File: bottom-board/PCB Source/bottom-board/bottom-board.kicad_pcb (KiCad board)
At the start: 2 copper layers, 193 x 93 mm, 259 parts, among them P1 USB_B, P10 JACK_TRS_6PINS, P11 JACK_TRS_6PINS, P12 JACK_TRS_6PINS, P13 RJ45, P14 AudioJack3, P2 USB_A, P3 BARREL_JACK, P5 HMI_DATA, P6 AudioJack3, P7 AudioJack3, P8 SERIAL_DEBUG, P9 JACK_TRS_6PINS, Q1 2N7002, Q10 J110, Q12 2N7002, Q13 2N7002, Q2 2N7002, Q3 J110, Q4 J110, Q5 J110, Q6 J110, Q7 2N7002, Q8 2N7002, Q9 J110, U1 TS2596, U10 RT9742MNGJ5, U11 6N137S, U12 ISL83491, U13 AP2120N-3.3, U2 LD1117S50TR_SOT223, U3 CS4265, U4 AT24CS08-STUM, U5 LM4562, U6 TL082, U7 TL082, U8 LM4811, U9 GR30-SOM

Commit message: rev 0.0.3
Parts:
- removed FB11, FB2, FB3, FB4, FB5, FB6, FB7, FB8, FB9: Ferrite_Bead, Resistor_SMD:R_0603_1608Metric
- removed G***: LOGO, Uno:mod-logo
- removed L3: 1mH, Inductor_SMD:L_Bourns_SRR1260
- removed R72: 10K, Resistor_SMD:R_0603_1608Metric
- added C73: 100nF, Capacitor_SMD:C_0603_1608Metric, F.Cu at (220.6, 99.7)
- added C75: 100nF, Capacitor_SMD:C_0603_1608Metric, F.Cu at (229.8, 102.1)
- added C76: 10uF, Capacitor_SMD:C_0805_2012Metric, F.Cu at (228.7, 105.5)
- added C77: 100nF, Capacitor_SMD:C_0603_1608Metric, F.Cu at (228.4, 103.7)
- added C78: 10uF, Capacitor_SMD:C_0805_2012Metric, F.Cu at (231.7, 98.1)
- added C79: 100nF, Capacitor_SMD:C_0603_1608Metric, F.Cu at (221.1, 94.9)
- added C80: 10uF, Capacitor_SMD:C_0805_2012Metric, F.Cu at (219.3, 94.9)
- added C81: 100nF, Capacitor_SMD:C_0603_1608Metric, F.Cu at (229.9, 97.9)
- added C82: 100nF, Capacitor_SMD:C_0603_1608Metric, F.Cu at (190.7, 64.0)
- added C83: 47uF, Capacitor_SMD:CP_Elec_5x5.4, F.Cu at (184.8, 93.8)
- added C84: 47uF, Capacitor_SMD:CP_Elec_5x5.4, F.Cu at (174.6, 111.0)
- added C85: 100nF, Capacitor_SMD:C_0603_1608Metric, F.Cu at (113.1, 66.9)
- added C86: 100nF, Capacitor_SMD:C_0603_1608Metric, F.Cu at (115.8, 70.0)
- added C87: 100nF, Capacitor_SMD:C_0603_1608Metric, F.Cu at (171.3, 82.8)
- added C88: 10uF, Capacitor_SMD:CP_Elec_4x5.7, F.Cu at (216.1, 101.3)
- added C89: 10uF, Capacitor_SMD:CP_Elec_4x5.7, F.Cu at (216.1, 106.2)
- added C90: 100pF, Capacitor_SMD:C_0603_1608Metric, F.Cu at (216.8, 98.0)
- added C91: 100pF, Capacitor_SMD:C_0603_1608Metric, F.Cu at (213.0, 109.8)
- added C92: 1nF, Capacitor_SMD:C_0603_1608Metric, F.Cu at (147.8, 52.2)
- added C93: 1nF, Capacitor_SMD:C_0603_1608Metric, F.Cu at (119.8, 44.2)
- added C94: 100nF, Capacitor_SMD:C_0603_1608Metric, F.Cu at (230.9, 110.3)
- added D12: BAT54S, Package_TO_SOT_SMD:SOT-23, F.Cu at (191.2, 57.8)
- added D17: BAT54S, Package_TO_SOT_SMD:SOT-23, F.Cu at (106.0, 67.6)
- added D18: BAT54S, Package_TO_SOT_SMD:SOT-23, F.Cu at (115.7, 72.8)
- added D19: BAT54S, Package_TO_SOT_SMD:SOT-23, F.Cu at (201.4, 101.6)
- added D20: BAT54S, Package_TO_SOT_SMD:SOT-23, F.Cu at (206.4, 110.2)
- added D21: BAT54S, Package_TO_SOT_SMD:SOT-23, F.Cu at (192.6, 96.2)
- added D22: BAT54S, Package_TO_SOT_SMD:SOT-23, F.Cu at (199.1, 106.1)
- added H6: MountingHole_Pad, MountingHole:MountingHole_3.2mm_M3_DIN965_Pad, F.Cu at (134.7, 83.7)
- added H7: MountingHole_Pad, MountingHole:MountingHole_3.2mm_M3_DIN965_Pad, F.Cu at (71.2, 83.7)
- added J1: AS0A823-H4SB-7H, Uno:TE_2309407-1, F.Cu at (106.2, 128.3)
- added JP1: Jumper, Jumper:SolderJumper-2_P1.3mm_Bridged2Bar_RoundedPad1.0x1.5mm, F.Cu at (225.6, 104.7)
- added R100: 1k, Resistor_SMD:R_0603_1608Metric, F.Cu at (195.0, 89.5)
- added R101: 100, Resistor_SMD:R_0603_1608Metric, F.Cu at (204.2, 77.5)
- added R102: 150R, Resistor_SMD:R_0603_1608Metric, F.Cu at (192.2, 93.5)
- added R103: 6R8, Resistor_SMD:R_0603_1608Metric, F.Cu at (108.2, 56.8)
- added R104: 6R8, Resistor_SMD:R_0603_1608Metric, F.Cu at (119.5, 50.9)
- added R105: 150R, Resistor_SMD:R_0603_1608Metric, F.Cu at (194.7, 102.7)
- added R106: 150R, Resistor_SMD:R_0603_1608Metric, F.Cu at (195.6, 106.8)
- added R107: 150R, Resistor_SMD:R_0603_1608Metric, F.Cu at (198.8, 111.2)
- added R108: 150R, Resistor_SMD:R_0603_1608Metric, F.Cu at (189.7, 94.5)
- added R109: 150R, Resistor_SMD:R_0603_1608Metric, F.Cu at (193.0, 108.5)
- added R48: 1M 1%, Resistor_SMD:R_0603_1608Metric, F.Cu at (119.8, 47.3)
- added R98: 10K, Resistor_SMD:R_0603_1608Metric, F.Cu at (201.9, 105.4)
- added R99: 1k, Resistor_SMD:R_0603_1608Metric, F.Cu at (245.0, 80.0)
- added X1: 24.576MHz, Oscillator:Oscillator_SMD_Abracon_ASV-4Pin_7.0x5.1mm, F.Cu at (226.6, 110.9)
- C1: value 100nF -> 10uF; footprint Capacitor_SMD:C_0603_1608Metric -> Capacitor_SMD:CP_Elec_4x5.7
- C11: value 10uF -> 100nF; footprint Capacitor_SMD:C_0805_2012Metric -> Capacitor_SMD:C_0603_1608Metric
- C14, C35, C38: value 10uF -> 100nF
- C2: value 1000uF -> 10uF; footprint Capacitor_THT:CP_Radial_D10.0mm_P5.00mm -> Capacitor_SMD:CP_Elec_4x5.7
- C24: footprint Capacitor_SMD:C_0805_2012Metric -> Capacitor_SMD:C_0603_1608Metric
- C4: value 100nF -> 1nF
- C40, C47, C55: value 10uF -> 100pF; footprint Capacitor_SMD:CP_Elec_4x5.7 -> Capacitor_SMD:C_0603_1608Metric
- C42: value 10uF -> 47uF; footprint Capacitor_SMD:CP_Elec_4x5.7 -> Capacitor_SMD:CP_Elec_5x5.4
- C53, C6: value 1000uF -> 100nF; footprint Capacitor_THT:CP_Radial_D10.0mm_P5.00mm -> Capacitor_SMD:C_0603_1608Metric
- C56: value 100uF -> 100pF; footprint Capacitor_SMD:CP_Elec_6.3x7.7 -> Capacitor_SMD:C_0603_1608Metric
- C57: value 100uF -> 47uF; footprint Capacitor_SMD:CP_Elec_6.3x7.7 -> Capacitor_SMD:CP_Elec_5x5.4
- C61: footprint Capacitor_SMD:CP_Elec_5x5.3 -> Capacitor_SMD:CP_Elec_4x5.7
- C72: value 100nF -> 47uF; footprint Capacitor_SMD:C_0603_1608Metric -> Capacitor_SMD:CP_Elec_5x5.4
- C74: value 1000uF -> 47uF; footprint Capacitor_THT:CP_Radial_D10.0mm_P5.00mm -> Capacitor_SMD:CP_Elec_5x5.4
- D15, D16: footprint Diode_SMD:D_SOD-523 -> Diode_SMD:D_SOD-323
- D3, D4: value 1N4148 -> BAT54S; footprint Diode_SMD:D_SOD-323 -> Package_TO_SOT_SMD:SOT-23
- H1: value MountingHole_Pad -> HOLE; footprint MountingHole:MountingHole_3.2mm_M3_DIN965_Pad -> Uno:Hole_3.5mm
- Q10, Q3, Q4, Q5, Q6, Q9: value J110 -> BSR58
- R1, R11, R2: value 10k -> 2k7
- R16: value 10K -> 1M 1%
- R42: value 5K6 -> 10K
- R43: value 10k -> 15K
- R68, R69: value 10K -> 2k7
- R70, R71: value 10K -> 1k
- R8: value 10R -> 100; footprint Resistor_SMD:R_1206_3216Metric -> Resistor_SMD:R_0603_1608Metric
- R80, R82, R84: value 33R -> 10K
- R81, R83: value 22K 1% -> 10K
- R85: value 68R -> 10K
- R86: value 33R -> 150R
- R87: value 68R -> 150R
- U2: value LD1117S50TR_SOT223 -> TL750M10CKVURG3; footprint Package_TO_SOT_SMD:SOT-223-3_TabPin2 -> Package_TO_SOT_SMD:TO-252-3_TabPin2
- U6, U7: value TL082 -> OPA1678
- U9: value GR30-SOM -> LD1117S50TR_SOT223; footprint gr-30:GR30SOM -> Package_TO_SOT_SMD:SOT-223-3_TabPin2
- moved R68 132.8 mm to (82.2, 119.0), turned to 270 degrees
- moved R6 127.6 mm to (96.7, 118.7)
- moved R4 126.5 mm to (94.5, 118.6)
- moved H5 126.5 mm to (249.3, 120.8)
- moved H1 126.4 mm to (147.9, 45.1)
- moved R7 124.1 mm to (98.5, 118.7)
- moved R69 123.6 mm to (90.8, 117.3), turned to 90 degrees
- moved R5 122.1 mm to (103.9, 118.8), turned to 180 degrees
- moved C72 96.5 mm to (202.7, 73.7), turned to 180 degrees
- moved C4 84.5 mm to (88.2, 117.3)
- moved U9 80.7 mm to (166.9, 84.1), turned to 90 degrees
- moved C74 80.5 mm to (213.2, 94.3)
- moved C53 70.2 mm to (192.6, 86.6), turned to 90 degrees
- moved R16 66.6 mm to (148.4, 49.8), turned to 90 degrees
- moved C6 65.1 mm to (197.2, 86.5), turned to 270 degrees
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- renumbered Power to Power1, Reset to Reset1
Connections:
- C1 pad 1: Net-(C1-Pad1) -> +10V
- C1 pad 2: GNDD -> GNDA
- C10 pad 1: +5VA -> +10V
- C11 pad 1: +5VA -> Net-(C11-Pad1)
- C13 pad 1: GNDD -> Net-(C13-Pad1)
- C13 pad 2: GNDA -> INPUT_BIAS
- C14 pad 1: GNDA -> Net-(C14-Pad1)
- C14 pad 2: Net-(C14-Pad2) -> INPUT_BIAS
- C2 pad 1: Net-(C1-Pad1) -> +5VA
- C2 pad 2: GNDD -> GNDA
- C22 pad 1: Net-(C14-Pad2) -> Net-(C22-Pad1)
- C22 pad 2: GNDA -> INPUT_BIAS
- C35 pad 1: GNDA -> Net-(C35-Pad1)
- C36 pad 1: Net-(C36-Pad1) -> +10V
- C37 pad 2: Net-(C36-Pad1) -> +10V
- C38 pad 1: GNDA -> Net-(C38-Pad1)
- C38 pad 2: OUTPUT_BIAS -> GNDA
- C39 pad 1: Net-(C39-Pad1) -> +10V
- C4 pad 1: +12VA -> GNDD
- C4 pad 2: GNDD -> +3V3
- C40 pad 1: CODEC_DAC_A -> Net-(C40-Pad1)
- C41 pad 2: Net-(C39-Pad1) -> +10V
- C42 pad 1: CODEC_DAC_B -> Net-(C42-Pad1)
- C43 pad 1: Net-(C39-Pad1) -> +10V
- C44 pad 1: Net-(C44-Pad1) -> GNDA
- C45 pad 2: Net-(C39-Pad1) -> +10V
- C47 pad 1: Net-(C47-Pad1) -> GNDA
- C53 pad 1: Net-(C1-Pad1) -> Net-(C53-Pad1)
- C53 pad 2: GNDD -> GNDA
- C55 pad 1: Net-(C55-Pad1) -> GNDA
- C56 pad 1: Net-(C56-Pad1) -> GNDA
- C6 pad 1: +12VA -> Net-(C6-Pad1)
- C6 pad 2: GNDD -> GNDA
- C69 pad 2: Net-(C69-Pad2) -> GNDA
- C72 pad 1: +1V8 -> INPUT_BIAS
- C72 pad 2: GNDD -> GNDA
- C74 pad 1: +12VA -> OUTPUT_BIAS
- C74 pad 2: GNDD -> GNDA
- C8 pad 1: +12VA -> Net-(C8-Pad1)
- C8 pad 2: GNDA -> GNDD
- C9 pad 1: +12VA -> Net-(C8-Pad1)
- C9 pad 2: GNDA -> GNDD
- D1 pad 1: Net-(C1-Pad1) -> Net-(C8-Pad1)
- D10 pad 2: Net-(D10-Pad2) -> +5VA
- D11 pad 2: Net-(D10-Pad2) -> +5VA
- D3 pad 2: GNDD -> +10V
- D4 pad 1: GNDD -> GNDA
- D4 pad 2: GNDA -> +10V
- D5 pad 2: Net-(D5-Pad2) -> Net-(C13-Pad1)
- D6 pad 2: Net-(D6-Pad2) -> Net-(C14-Pad1)
- D8 pad 2: Net-(D8-Pad2) -> Net-(C22-Pad1)
- D9 pad 2: Net-(D9-Pad2) -> Net-(C35-Pad1)
- P1 pad 1: Net-(FB6-Pad1) -> Net-(C49-Pad1)
- P1 pad 2: Net-(FB7-Pad1) -> USB_DEV_DM
- P1 pad 3: Net-(FB8-Pad1) -> USB_DEV_DP
- P1 pad 4: Net-(FB9-Pad1) -> GNDD
- P1 pad 5: GNDD -> Net-(C92-Pad2)
- P11 pad R: Net-(P11-PadR) -> Net-(C83-Pad2)
- P11 pad T: Net-(P11-PadT) -> Net-(C42-Pad2)
- P12 pad R: Net-(P12-PadR) -> Net-(C84-Pad2)
- P12 pad T: Net-(P12-PadT) -> Net-(C57-Pad2)
- P14 pad R: Net-(C71-Pad2) -> Net-(P14-PadR)
- P14 pad T: Net-(C70-Pad2) -> Net-(P14-PadT)
- P2 pad 5: GNDD -> Net-(C93-Pad2)
- P5 pad 10: +12V -> Net-(P5-Pad10)
- P5 pad 13: POWER_BUTTON -> HMI_ISP_ENABLE
- P5 pad 14: HMI_ISP_ENABLE -> POWER_BUTTON
- P5 pad 15: PM_LEDS_OE -> HMI_RESET
- P5 pad 16: HMI_RESET -> PM_LEDS_OE
- P5 pad 17: PM_LEDS_SCL -> HMI_UART_TX
- P5 pad 18: HMI_UART_TX -> PM_LEDS_SCL
- P5 pad 19: PM_LEDS_SDA -> HMI_UART_RX
- P5 pad 20: HMI_UART_RX -> PM_LEDS_SDA
- P5 pad 3: HMI_RFU_TX -> +12V
- P5 pad 4: +12V -> HMI_RFU_TX
- P5 pad 5: HMI_RFU_RX -> +12V
- P5 pad 6: +12V -> HMI_RFU_RX
- P5 pad 7: Net-(P5-Pad7) -> +12V
- P5 pad 8: +12V -> Net-(P5-Pad8)
- P5 pad 9: Net-(P5-Pad9) -> +12V
- Q1 pad 1: IN2_GC1 -> Net-(C6-Pad1)
- Q2 pad 1: IN1_GC1 -> Net-(C11-Pad1)
- Q3 pad 3: Net-(D5-Pad2) -> Net-(C13-Pad1)
- Q4 pad 3: Net-(D6-Pad2) -> Net-(C14-Pad1)
- Q5 pad 3: Net-(D8-Pad2) -> Net-(C22-Pad1)
- Q6 pad 3: Net-(D9-Pad2) -> Net-(C35-Pad1)
- Q7 pad 1: IN2_GC2 -> Net-(C53-Pad1)
- Q8 pad 1: IN1_GC2 -> Net-(C38-Pad1)
- R12 pad 1: Net-(P5-Pad7) -> Net-(P5-Pad8)
- R13 pad 1: Net-(P5-Pad9) -> Net-(P5-Pad10)
- R16 pad 1: UBOOT_BUTTON -> Net-(C92-Pad2)
- R16 pad 2: +1V8 -> GNDD
- R19 pad 1: IN2_GC1 -> Net-(C6-Pad1)
- R19 pad 2: +12VA -> +10V
- R20 pad 2: IN2_GC1 -> Net-(C6-Pad1)
- R21 pad 1: IN1_GC1 -> Net-(C11-Pad1)
- R21 pad 2: +12VA -> +10V
- R22 pad 2: IN1_GC1 -> Net-(C11-Pad1)
- R25 pad 2: +12VA -> +10V
- R26 pad 2: +12VA -> +10V
- R27 pad 2: Net-(D5-Pad2) -> Net-(C13-Pad1)
- R29 pad 2: Net-(D6-Pad2) -> Net-(C14-Pad1)
- R40 pad 2: Net-(D8-Pad2) -> Net-(C22-Pad1)
- R44 pad 2: Net-(D9-Pad2) -> Net-(C35-Pad1)
- R53 pad 2: +12VA -> +10V
- R54 pad 2: +12VA -> +10V
- R64 pad 1: IN2_GC2 -> Net-(C53-Pad1)
- R64 pad 2: +12VA -> +10V
- R65 pad 2: IN2_GC2 -> Net-(C53-Pad1)
- R66 pad 1: IN1_GC2 -> Net-(C38-Pad1)
- R66 pad 2: +12VA -> +10V
- R67 pad 2: IN1_GC2 -> Net-(C38-Pad1)
- R68 pad 1: INPUT_BIAS -> +3V3
- R68 pad 2: Net-(C36-Pad1) -> PM_LEDS_SCL
- R69 pad 1: GNDA -> PM_LEDS_SDA
- R69 pad 2: INPUT_BIAS -> +3V3
- R70 pad 1: OUTPUT_BIAS -> IN2_GC1
- R70 pad 2: Net-(C39-Pad1) -> Net-(C6-Pad1)
- R71 pad 1: GNDA -> IN1_GC1
- R71 pad 2: OUTPUT_BIAS -> Net-(C11-Pad1)
- R73 pad 1: Net-(C42-Pad2) -> Net-(C89-Pad1)
- R73 pad 2: Net-(C46-Pad2) -> Net-(C91-Pad1)
- R74 pad 1: Net-(C44-Pad2) -> Net-(C88-Pad1)
- R74 pad 2: Net-(C44-Pad1) -> Net-(C90-Pad1)
- R76 pad 1: Net-(C44-Pad1) -> Net-(C90-Pad1)
- R76 pad 2: Net-(R76-Pad2) -> OUTPUT_BIAS
- R77 pad 1: OUTPUT_BIAS -> Net-(C91-Pad1)
- R77 pad 2: Net-(C47-Pad1) -> OUTPUT_BIAS
- R79 pad 2: Net-(C55-Pad1) -> Net-(R79-Pad2)
- R8 pad 1: GNDA -> OUTPUT_BIAS
- R8 pad 2: GNDD -> +5VA
- R80 pad 1: GNDA -> OUTPUT_BIAS
- R80 pad 2: Net-(C47-Pad2) -> Net-(C40-Pad2)
- R81 pad 1: GNDA -> Net-(C40-Pad1)
- R81 pad 2: Net-(C56-Pad2) -> Net-(R81-Pad2)
- R82 pad 1: GNDA -> OUTPUT_BIAS
- R82 pad 2: Net-(C55-Pad2) -> Net-(R82-Pad2)
- R83 pad 1: GNDA -> OUTPUT_BIAS
- R83 pad 2: Net-(C57-Pad2) -> Net-(C46-Pad2)
- R84 pad 1: Net-(C47-Pad2) -> Net-(C40-Pad2)
- R84 pad 2: Net-(P11-PadR) -> Net-(C40-Pad1)
- R85 pad 1: Net-(C56-Pad2) -> Net-(R81-Pad2)
- R85 pad 2: Net-(P11-PadT) -> Net-(D21-Pad3)
- R86 pad 1: Net-(C55-Pad2) -> Net-(C40-Pad1)
- R86 pad 2: Net-(P12-PadR) -> Net-(C44-Pad2)
- R87 pad 1: Net-(C57-Pad2) -> Net-(C46-Pad1)
- R87 pad 2: Net-(P12-PadT) -> Net-(C47-Pad2)
- U2 pad 1: GNDA -> Net-(C8-Pad1)
- U2 pad 2: +5VA -> GNDA
- U2 pad 3: +12VA -> +10V
- U3 pad 14: CODEC_ADC_A -> (no net)
- U3 pad 15: CODEC_ADC_B -> (no net)
- U3 pad 17: Net-(D10-Pad2) -> +5VA
- U3 pad 5: Net-(D10-Pad2) -> +5VA
- U3 pad 9: Net-(FB2-Pad1) -> GNDA
- U5 pad 8: Net-(C36-Pad1) -> +10V
- U6 pad 1: Net-(C44-Pad1) -> Net-(C40-Pad1)
- U6 pad 2: Net-(C44-Pad2) -> Net-(C40-Pad2)
- U6 pad 3: OUTPUT_BIAS -> Net-(C90-Pad1)
- U6 pad 5: Net-(C47-Pad1) -> Net-(R82-Pad2)
- U6 pad 6: Net-(R76-Pad2) -> Net-(R81-Pad2)
- U6 pad 7: Net-(C56-Pad1) -> Net-(D21-Pad3)
- U6 pad 8: Net-(C39-Pad1) -> +10V
- U7 pad 3: OUTPUT_BIAS -> Net-(C91-Pad1)
- U7 pad 5: Net-(C55-Pad1) -> Net-(R79-Pad2)
- U7 pad 7: Net-(C57-Pad1) -> Net-(D22-Pad3)
- U7 pad 8: Net-(C39-Pad1) -> +10V
- U8 pad 5: Net-(C69-Pad2) -> GNDA
- U9 pad 1: HP_VOL -> +10V
- U9 pad 2: HP_CLOCK -> GNDA
- U9 pad 3: MIDI_UART_RX -> +5VA
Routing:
- net GNDA: track 209.3 -> 3888.9 mm, vias 35 -> 70
- net +10V: track 0.00 -> 309.0 mm, vias 0 -> 5
- net +12VA: track 241.3 -> 0.00 mm, vias 2 -> 0
- net CODEC_I2S_SDOUT: track 179.5 -> 9.65 mm
- net CODEC_I2S_LRCK: track 181.4 -> 13.2 mm
- net CODEC_I2S_BCLK: track 181.4 -> 14.2 mm
- net CODEC_I2S_SDIN: track 177.3 -> 12.2 mm
- net Net-(R6-Pad1): track 2.17 -> 145.4 mm
- net Net-(R4-Pad2): track 7.31 -> 149.0 mm
- net Net-(P11-PadT): track 140.1 -> 0.00 mm, vias 2 -> 0
- net Net-(R7-Pad1): track 3.54 -> 142.2 mm
- net Net-(C83-Pad2): track 0.00 -> 136.9 mm, vias 0 -> 2
- net Net-(R5-Pad1): track 1.84 -> 137.2 mm
- net Net-(C84-Pad2): track 0.00 -> 134.6 mm, vias 0 -> 2
- net Net-(C42-Pad2): track 3.26 -> 131.4 mm, vias 0 -> 2
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- removed copper zone on F.Cu, net +5V
- removed copper zone on F.Cu, net GNDA
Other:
- outline, holes or cut-outs redrawn
- board text added: "260P DDR4 5.2 STD Connector"
- board text added: "Cut Layer"
- board text added: "Firefly PX30 SoM"
- board text added: "Foot Switches [8-14mm clearance]"
- board text added: "HMI Cable Connector (TOP) [4.6mm clearance]"
- board text added: "HMI Center Line"
- board text added: "HMI Receptical (TOP) [8.7mm clearance]"
- board text added: "Jacks"
- board text added: "MOD Devices GmbH http://moddevices.com [MDW-ELE-001] MOD Dwarf - Main Board Rev.: MDW-PX30-V0.03 Date: 2020.09.18"
- board text added: "Screw Bosses [0mm clearance]"
- board text removed: "MOD Devices GmbH http://moddevices.com [DW-ELE-001] MOD Dwarf - Main Board Rev.: 2020.07.07"

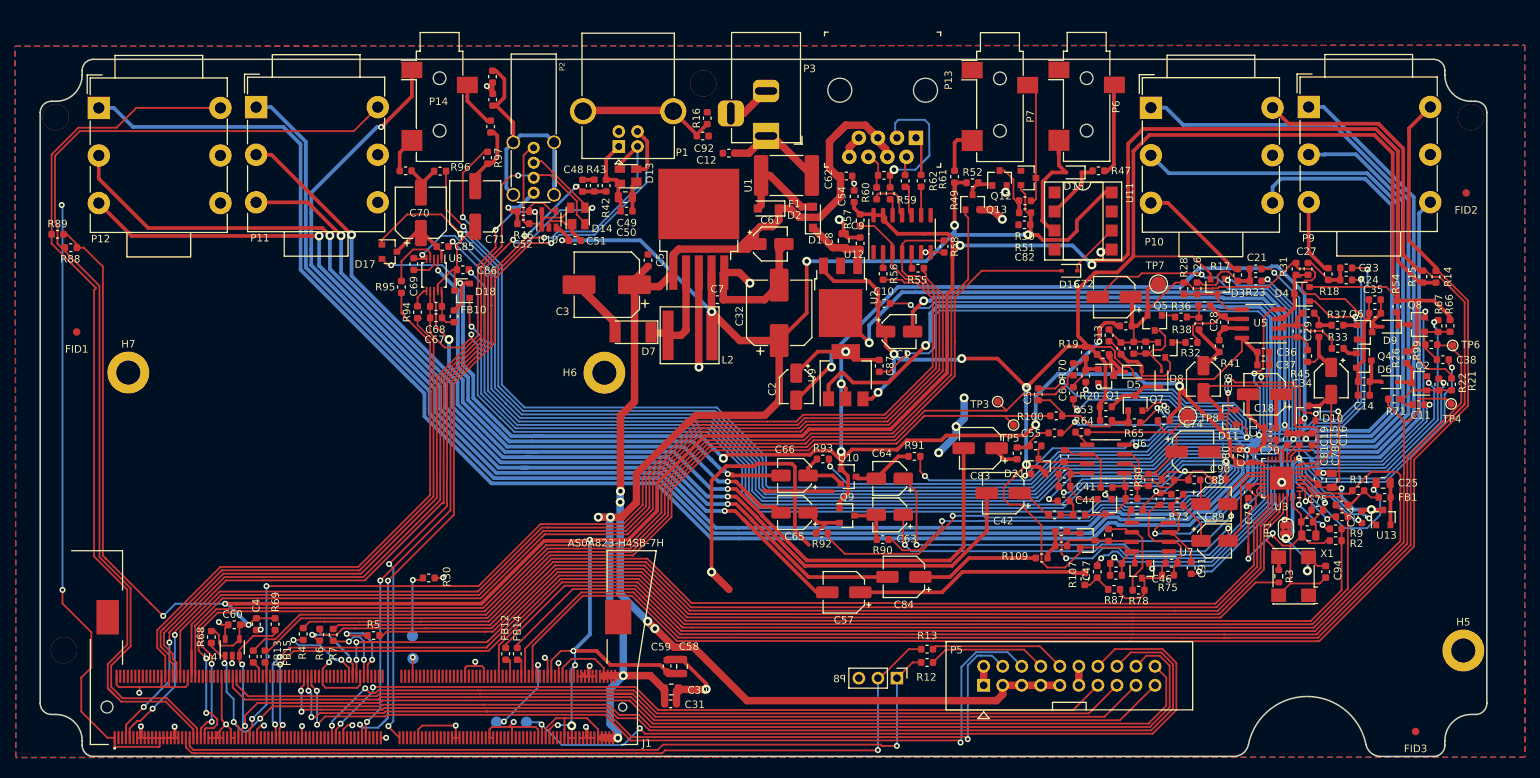
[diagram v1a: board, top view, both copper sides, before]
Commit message: change design to 4 layer PCB
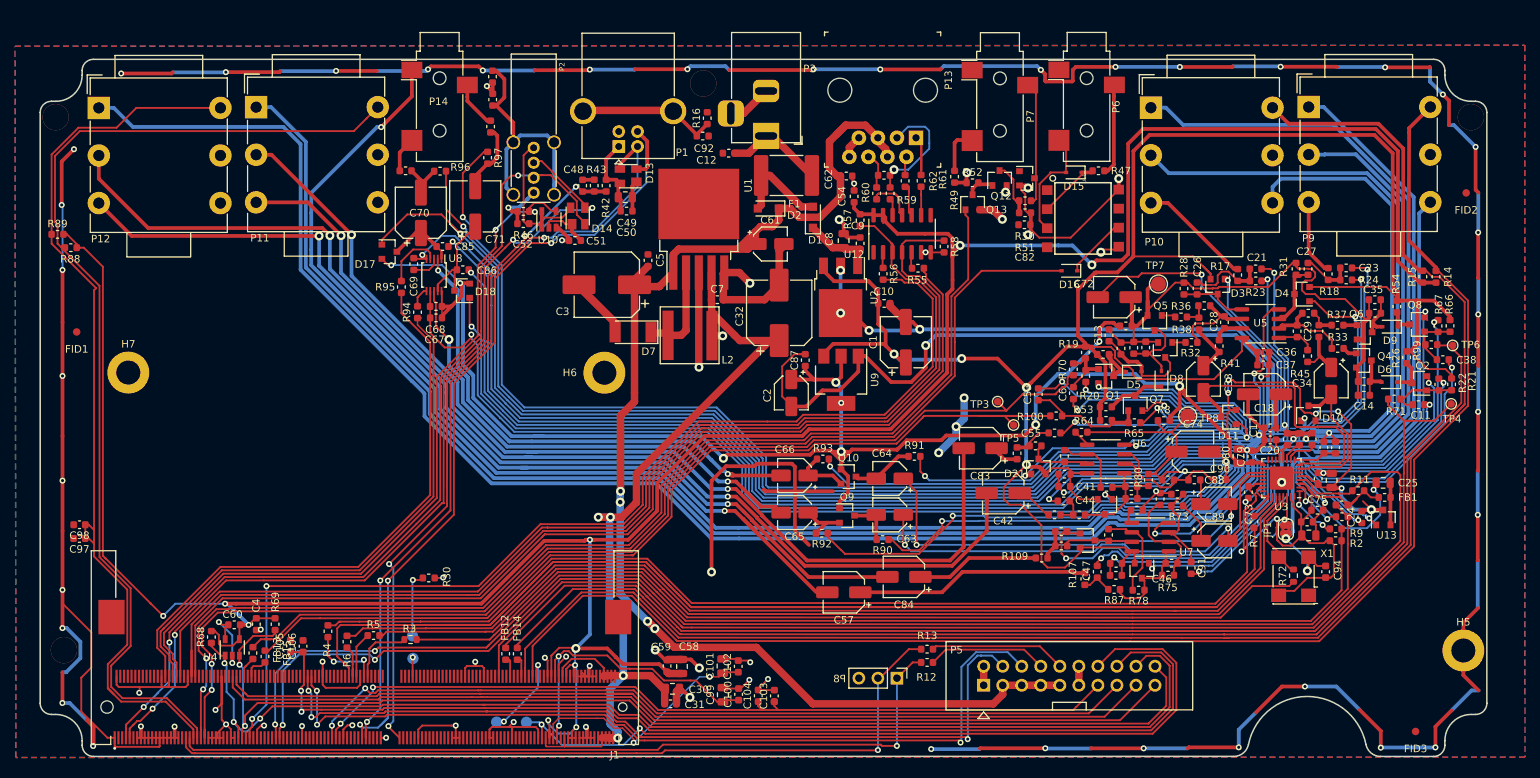
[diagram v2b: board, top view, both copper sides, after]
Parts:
- removed FB10: Ferrite_Bead, Resistor_SMD:R_0603_1608Metric
- added C100: 100nF, Capacitor_SMD:C_0603_1608Metric, F.Cu at (152.6, 126.6)
- added C101: 10uF, Capacitor_SMD:C_0805_2012Metric, F.Cu at (150.5, 122.9)
- added C102: 100nF, Capacitor_SMD:C_0603_1608Metric, F.Cu at (152.5, 122.9)
- added C103: 1uF, Capacitor_SMD:C_0603_1608Metric, F.Cu at (157.4, 126.9)
- added C104: 100nF, Capacitor_SMD:C_0603_1608Metric, F.Cu at (155.2, 126.8)
- added C105: 1uF, Capacitor_SMD:C_0603_1608Metric, F.Cu at (92.8, 120.2)
- added C106: 100nF, Capacitor_SMD:C_0603_1608Metric, F.Cu at (94.5, 120.2)
- added C95: 100nF, Capacitor_SMD:C_0603_1608Metric, F.Cu at (230.7, 93.7)
- added C96: 10uF, Capacitor_SMD:C_0603_1608Metric, F.Cu at (232.2, 93.7)
- added C97: 1uF, Capacitor_SMD:C_0603_1608Metric, F.Cu at (64.6, 105.8)
- added C98: 100nF, Capacitor_SMD:C_0603_1608Metric, F.Cu at (64.7, 104.0)
- added C99: 10uF, Capacitor_SMD:C_0805_2012Metric, F.Cu at (150.5, 126.7)
- added R72: 0R, Resistor_SMD:R_0603_1608Metric, F.Cu at (226.6, 110.8)
- C1: value 10uF -> 100uF; footprint Capacitor_SMD:CP_Elec_4x5.7 -> Capacitor_SMD:CP_Elec_6.3x7.7
- J1: footprint Uno:TE_2309407-1 -> Uno:TE_2309409-1
- Q10, Q3, Q4, Q5, Q6: value BSR58 -> MMBFJ201
- R1, R11, R2, R68, R69: value 2k7 -> 2K7
- R100, R70, R71, R99: value 1k -> 1K
- R101, R8: value 100 -> 100R
- R41, R45: value 100R 1% -> 100R
- R46, R51, R52, R57, R58: value 10k -> 10K
- R90, R91: value 1M -> 1M 1%
- U11: footprint Package_DIP:DIP-8_W7.62mm_SMDSocket_SmallPads -> Uno:6N137S
- moved R7 123.8 mm to (221.3, 103.6)
- moved R3 116.1 mm to (108.8, 119.3), turned to 180 degrees
- moved C87 9.90 mm to (161.5, 82.1), turned to 90 degrees
- moved R6 3.76 mm to (100.3, 119.6)
- moved R4 3.32 mm to (97.8, 118.2)
- moved C1 1.68 mm to (174.9, 79.7), turned to 90 degrees
- moved C2 1.07 mm to (159.6, 86.4)
- moved U9 0.87 mm to (166.3, 84.7), turned to 270 degrees
- moved FB13 0.46 mm to (87.8, 121.1)
- moved U11 0.23 mm to (198.7, 63.3), turned to 270 degrees
- moved D12 0.20 mm to (191.1, 57.8)
- moved C30 0.18 mm to (143.8, 125.9)
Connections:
- C67 pad 2: Net-(C67-Pad2) -> +5VA
- C68 pad 1: Net-(C67-Pad2) -> +5VA
- H6 pad 1: (no net) -> GNDD
- H7 pad 1: (no net) -> GNDD
- J1 pad 126: CODEC_I2S_SDIN -> CODEC_I2S_SDOUT
- J1 pad 130: CODEC_I2S_MCLK -> CODEC_I2S_LRCK
- J1 pad 134: CODEC_I2S_SDOUT -> CODEC_I2S_SDIN
- J1 pad 136: CODEC_I2S_LRCK -> CODEC_I2S_MCLK
- J1 pad 227: (no net) -> +3V0
- J1 pad 228: (no net) -> +1V8
- J1 pad 229: (no net) -> +1V8
- J1 pad 234: (no net) -> +3V3
- J1 pad 47: MIDI_UART_RX -> MIDI_UART_TX
- J1 pad 49: MIDI_UART_TX -> MIDI_UART_RX
- J1 pad 70: (no net) -> Net-(FB13-Pad1)
- J1 pad 74: (no net) -> Net-(FB15-Pad1)
- J1 pad 78: Net-(FB13-Pad1) -> (no net)
- J1 pad 82: Net-(FB15-Pad1) -> (no net)
- U3 pad 29: Net-(R3-Pad1) -> Net-(R72-Pad2)
- U3 pad 9: GNDA -> Net-(C95-Pad1)
- U8 pad 10: Net-(C67-Pad2) -> +5VA
- U9 pad 1: +10V -> GNDA
- U9 pad 2: GNDA -> +5VA
- U9 pad 3: +5VA -> +10V
- X1 pad 3: Net-(R3-Pad1) -> Net-(R72-Pad2)
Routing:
- net GNDD: track 368.7 -> 839.1 mm, vias 38 -> 78
- net GNDA: track 3888.9 -> 3563.6 mm, vias 70 -> 69
- net CODEC_I2S_SDOUT: track 9.65 -> 273.6 mm, vias 2 -> 0
- net Net-(R7-Pad1): track 142.2 -> 4.31 mm
- net CODEC_I2S_MCLK: track 140.8 -> 8.97 mm, vias 2 -> 0
- net Net-(R3-Pad1): track 11.3 -> 125.1 mm
- net +5V: track 230.6 -> 153.6 mm, vias 9 -> 10
- net +1V8: track 0.00 -> 41.1 mm, vias 0 -> 2
- net +3V0: track 0.00 -> 32.4 mm, vias 0 -> 2
- net Net-(R72-Pad2): track 0.00 -> 12.3 mm
- net CODEC_I2S_BCLK: track 14.2 -> 5.15 mm, vias 2 -> 0
- net CODEC_I2S_LRCK: track 13.2 -> 6.07 mm, vias 2 -> 0
- net +5VA: track 279.3 -> 286.5 mm
- net +3V3: track 387.5 -> 394.6 mm
- net Net-(C95-Pad1): track 0.00 -> 6.19 mm
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- added copper zone on PWR-5VD.Cu, net +5V
- added copper zone on GNDD.Cu, net GNDD
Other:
- copper layers 2 -> 4

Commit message: change posistion of connectors a tiny bit, now locked in place
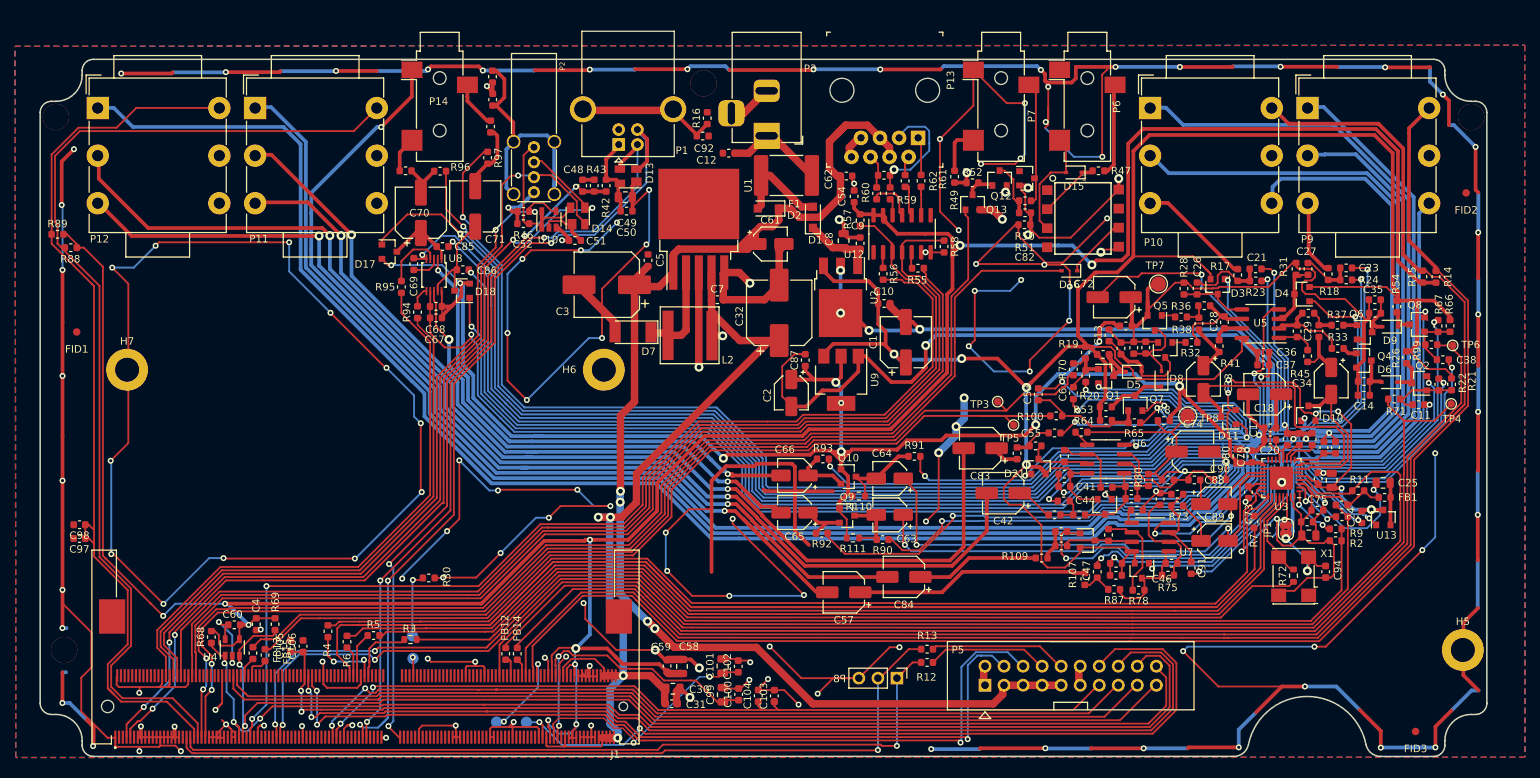
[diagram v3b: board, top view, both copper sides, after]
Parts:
- added R110: 1M 1%, Resistor_SMD:R_0603_1608Metric, F.Cu at (168.6, 100.2)
- added R111: 1M 1%, Resistor_SMD:R_0603_1608Metric, F.Cu at (167.8, 105.8)
- Q10, Q3, Q4, Q5, Q6: value MMBFJ201 -> MMBFJ111
- Q9: value BSR58 -> MMBFJ111
- moved H7 0.42 mm to (71.0, 83.3)
- moved H6 0.41 mm to (134.6, 83.3)
- moved P13 0.29 mm to (176.5, 52.4)
- moved P1 0.26 mm to (136.6, 53.3)
- moved P9 0.21 mm to (228.5, 61.1)
- moved FB15 0.19 mm to (89.4, 121.4)
- moved P11 0.18 mm to (88.1, 61.1)
- moved P5 0.18 mm to (185.5, 125.4)
- moved P7 0.16 mm to (187.6, 46.9)
- moved C31 0.16 mm to (143.7, 127.9)
- moved P12 0.15 mm to (67.1, 61.1)
- moved J1 0.12 mm to (106.3, 128.3)
- moved P10 0.12 mm to (207.5, 61.1)
- moved H5 0.10 mm to (249.2, 120.7)
- moved P6 0.09 mm to (199.1, 46.9)
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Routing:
- net GNDD: track 839.1 -> 1462.4 mm, vias 78 -> 140
- net RS485_TX+: track 10.5 -> 6.62 mm
- net CHAIN_UART_DE: track 152.2 -> 148.7 mm
- net +5VA: track 286.5 -> 290.0 mm
- net HMI_UART_TX: track 128.6 -> 125.4 mm
- net Net-(C64-Pad2): track 8.33 -> 11.4 mm
- net USB_HOST_DP: track 125.0 -> 122.0 mm
- net Net-(C63-Pad2): track 6.18 -> 8.62 mm
- net +3V3: track 394.6 -> 392.3 mm
- net +5V: track 153.6 -> 151.8 mm
- net MIDI_UART_RX: track 159.3 -> 158.0 mm
- net MIDI_UART_TX: track 156.3 -> 155.0 mm
- net PM_LEDS_SDA: track 151.6 -> 152.8 mm
- net USB_DEV_DM: track 103.8 -> 102.7 mm
- net +12V: track 173.1 -> 174.2 mm
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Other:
- board text removed: "260P DDR4 5.2 STD Connector"
- board text removed: "Cut Layer"
- board text removed: "Firefly PX30 SoM"
- board text removed: "Foot Switches [8-14mm clearance]"
- board text removed: "HMI Cable Connector (TOP) [4.6mm clearance]"
- board text removed: "HMI Center Line"
- board text removed: "HMI Receptical (TOP) [8.7mm clearance]"
- board text removed: "Jacks"
- board text removed: "Screw Bosses [0mm clearance]"
